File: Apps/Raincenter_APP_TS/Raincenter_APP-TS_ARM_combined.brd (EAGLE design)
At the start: 77.4 x 27.4 mm, 31 parts, among them IC101 MAX232ECSE

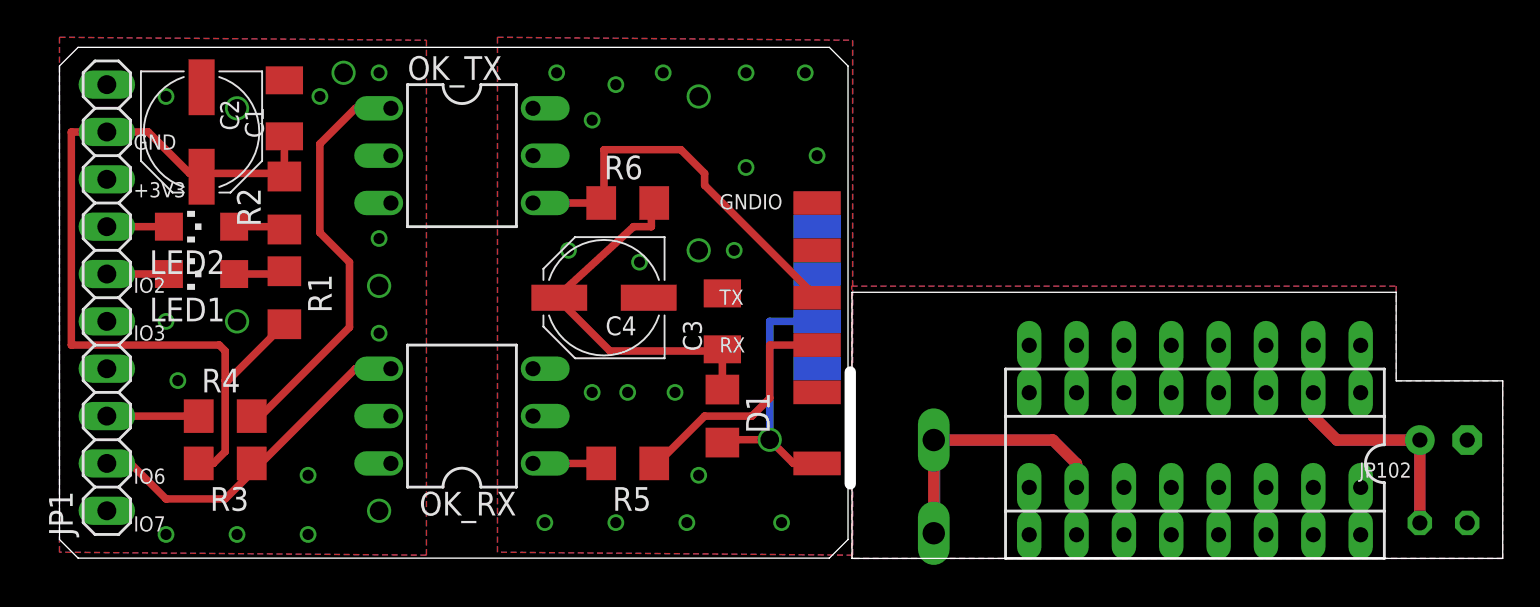
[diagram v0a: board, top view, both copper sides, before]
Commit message: Raincenter_APP updated combinded schematic and board (for cheaper production) of Raincenter_APP_TS_ARM_ISO_0.02 & Raincenter_MAX232_Adapter_0.02
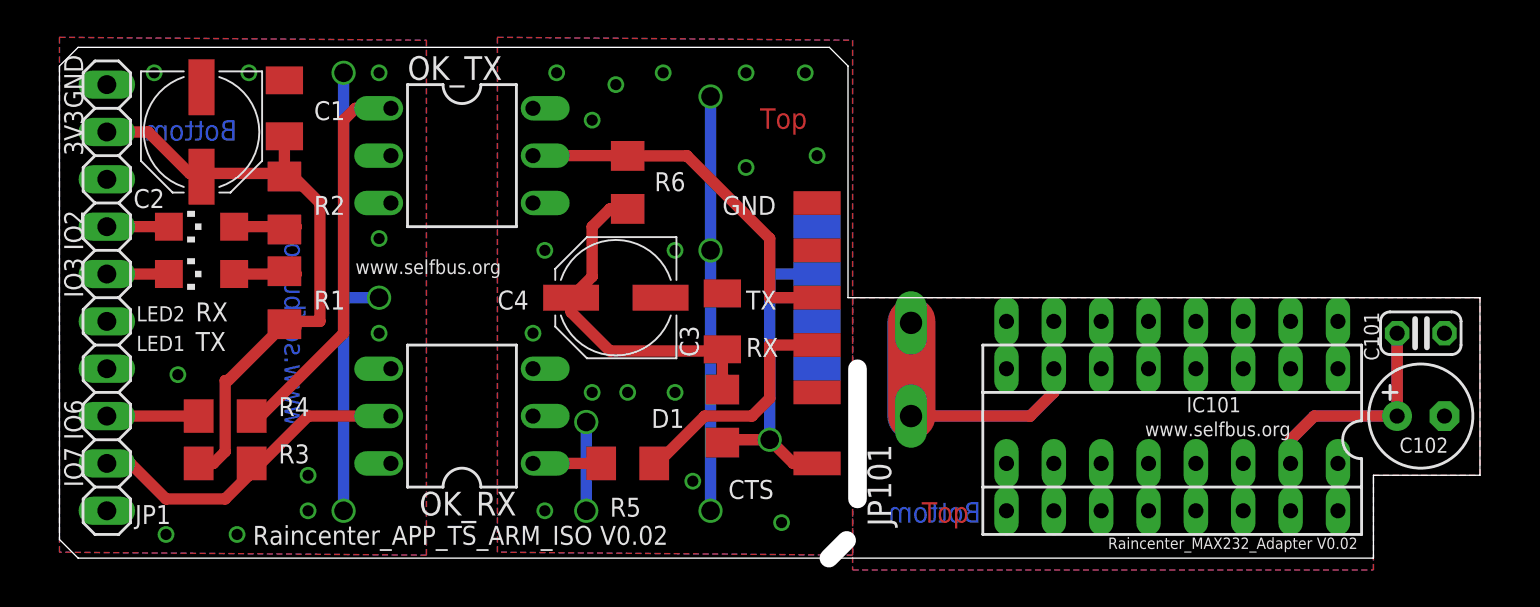
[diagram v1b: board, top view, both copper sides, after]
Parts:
- C2, C4: value 100µF 25V -> 100µF/25V
- LED1: value green -> RX-green
- LED2: value yellow -> TX-yellow
- PAD10: value RTS -> CTS
- PAD7: value RTS -> (none)
- PAD8: value (none) -> CTS
- R3: value 4K7 -> 2K7
- R6: value 2K2 -> 2K7
- moved C101 10.2 mm to (73.0, 12.1), flipped to the top, turned to 0 degrees
- moved JP102 4.01 mm to (59.7, 8.89), flipped to the bottom, turned to 0 degrees
- moved C102 1.77 mm to (73.0, 7.62), flipped to the top, turned to 0 degrees
- moved JP101 1.77 mm to (43.2, 7.62), flipped to the top, turned to 180 degrees
- moved IC101 1.75 mm to (59.7, 6.35), flipped to the top, turned to 180 degrees
- moved R6 1.11 mm to (30.5, 20.2), turned to 270 degrees
- moved C4 0.63 mm to (29.8, 14.0)
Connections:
- removed net RX_TX: OK_TX.4, PAD3.1, R6.1
- new net RC_TX: OK_TX.5, PAD3.1, R6.1
- net GND: now also OK_RX.4; no longer OK_RX.5
- net GNDIO: now also OK_TX.4; no longer OK_TX.5
- net IO7: now also OK_RX.5; no longer OK_RX.4
- net RC_RTS: now also PAD8.1; no longer PAD7.1
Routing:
- net GNDIO: track 0.00 -> 27.0 mm, vias 21 -> 22
- net GND: track 0.00 -> 25.4 mm, vias 16 -> 13
- net RX_TX: track 21.8 -> 0.00 mm
- net RC_TX: track 0.00 -> 20.3 mm
- net +3V3: track 47.4 -> 34.9 mm
- net RC_RTS: track 14.6 -> 17.2 mm
- net N$10: track 22.3 -> 21.0 mm
- net IO7: track 19.7 -> 18.7 mm
- net V+: track 20.1 -> 19.6 mm
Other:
- board size 77.4 x 27.4 mm -> 76.2 x 27.4 mm
- board text added: "3V3"
- board text added: "Bottom"
- board text added: "CTS"
- board text added: "GND"
- board text added: "IO2"
- board text added: "IO3"
- board text added: "IO6"
- board text added: "IO7"
- board text added: "RX"
- board text added: "Raincenter_APP_TS_ARM_ISO V0.02"
- board text added: "Raincenter_MAX232_Adapter V0.02"
- board text added: "TX"
- board text added: "Top"
- board text added: "www.selfbus.org"
- board text removed: "GND +3V3 IO2 IO3 IO6 IO7"
- board text removed: "GNDIO TX RX"
